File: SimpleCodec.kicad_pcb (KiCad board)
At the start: 4 copper layers, 59 x 93 mm, 119 parts, among them J1 RPI_ADC, J2 RP_GPIO, Q1 AO3401A, U1 AMS1117-5.0, U2 AMS1117-3.3, U3 NE5532, U4 NE5532, U5 NE5532, U6 NE5532, U7 NE5532, U8 CS4272, X1 PEDAL_COMBO_TOP

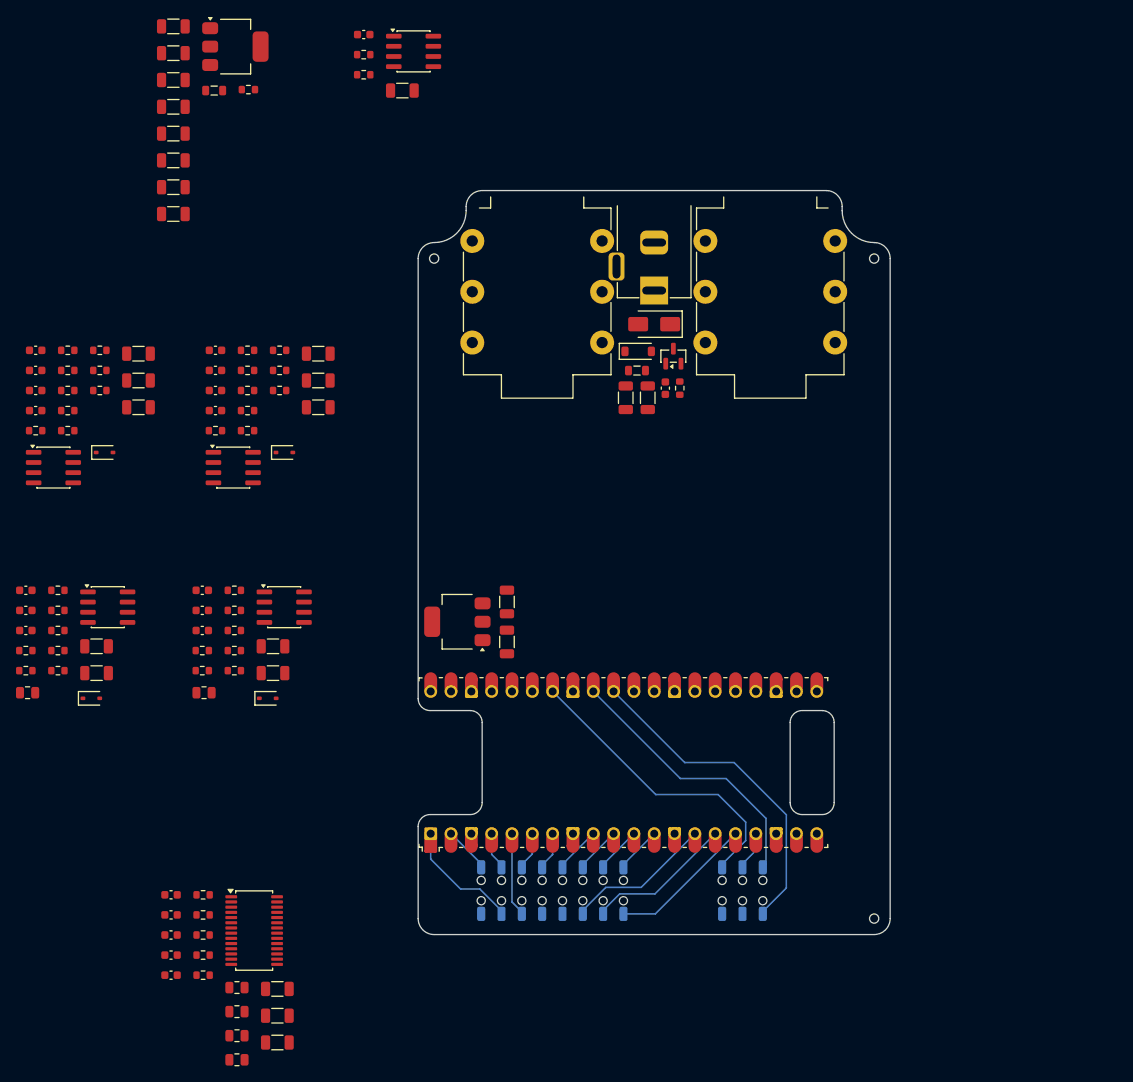
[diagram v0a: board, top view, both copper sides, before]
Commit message: Buffer and layout
Updated the input and output buffers.
Updated the board layout.
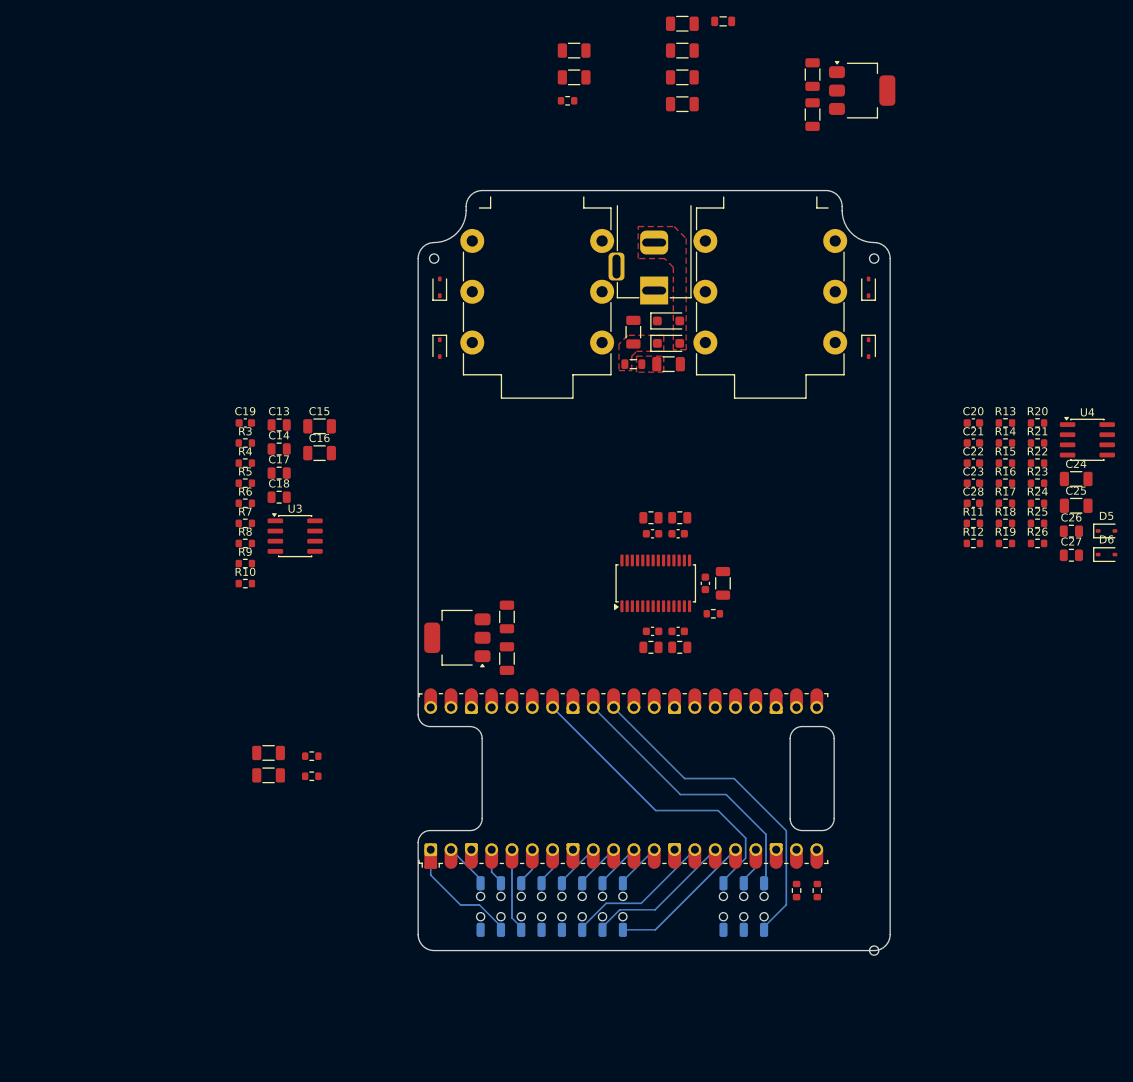
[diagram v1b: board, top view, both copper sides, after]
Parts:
- removed the C11 at (89.9, 42.1)
- removed the C2 at (151.4, 67.2)
- removed C41, C44, C45, C47, C48, C49: 100n, Capacitor_SMD:C_0603_1608Metric
- removed C42, C43, C51, C53: 1u, Capacitor_SMD:C_0805_2012Metric
- removed C46, C50: 4.7u, Capacitor_SMD:C_1206_3216Metric
- removed C52: 22u, Capacitor_SMD:C_1206_3216Metric
- removed the C8 at (89.9, 35.4)
- removed the D5 at (103.8, 75.2)
- removed the D6 at (81.3, 75.2)
- removed Q1: AO3401A, Package_TO_SOT_SMD:SOT-23
- removed R31: 22K, Resistor_SMD:R_0603_1608Metric
- removed R32, R33: 220, Resistor_SMD:R_0603_1608Metric
- removed R34, R35: 100, Resistor_SMD:R_0603_1608Metric
- removed R36, R37, R38, R39, R40, R41: 47K, Resistor_SMD:R_0603_1608Metric
- removed U6, U7: NE5532, Package_SO:SOIC-8_3.9x4.9mm_P1.27mm
- removed U8: CS4272, Package_SO:TSSOP-28_4.4x9.7mm_P0.65mm
- added C12: 22u, Capacitor_SMD:C_1206_3216Metric, F.Cu at (153.5, 31.7)
- added C6: 10u, Capacitor_SMD:C_1206_3216Metric, F.Cu at (169.8, 33.0)
- added C9: 4.7u, Capacitor_SMD:C_1206_3216Metric, F.Cu at (153.5, 25.0)
- added D5: H15VSD3B, Diode_SMD:D_SOD-323, F.Cu at (206.6, 85.0)
- added D5: H15VSD3B, Diode_SMD:D_SOD-323, F.Cu at (176.8, 62.2)
- added D6: H15VSD3B, Diode_SMD:D_SOD-323, F.Cu at (176.8, 54.6)
- added D6: H15VSD3B, Diode_SMD:D_SOD-323, F.Cu at (206.6, 88.0)
- C10: value 4.7u -> 22u
- C13: value 22u -> 2.2n; footprint Capacitor_SMD:C_1206_3216Metric -> Capacitor_SMD:C_0805_2012Metric
- C14: value 10u -> 2.2n; footprint Capacitor_SMD:C_1206_3216Metric -> Capacitor_SMD:C_0805_2012Metric
- C15: value 100n -> 10u; footprint Capacitor_SMD:C_0603_1608Metric -> Capacitor_SMD:C_1206_3216Metric
- C16: value 470p -> 10u; footprint Capacitor_SMD:C_0603_1608Metric -> Capacitor_SMD:C_1206_3216Metric
- C17: value 470p -> 2.2n; footprint Capacitor_SMD:C_0603_1608Metric -> Capacitor_SMD:C_0805_2012Metric
- C18: value 1u -> 2.2n
- C19: value 1u -> 100n; footprint Capacitor_SMD:C_0805_2012Metric -> Capacitor_SMD:C_0603_1608Metric
- C20, C21: value 2.2n -> 330p
- C22, C23: value 10u -> 330p; footprint Capacitor_SMD:C_1206_3216Metric -> Capacitor_SMD:C_0603_1608Metric
- C24, C25, C37: value 4.7u -> 10u
- C26, C27: value 100n -> 2.2n; footprint Capacitor_SMD:C_0603_1608Metric -> Capacitor_SMD:C_0805_2012Metric
- C28, C31, C36: value 4.7u -> 100n; footprint Capacitor_SMD:C_1206_3216Metric -> Capacitor_SMD:C_0603_1608Metric
- C29, C30: value 4.7u -> 1u; footprint Capacitor_SMD:C_1206_3216Metric -> Capacitor_SMD:C_0805_2012Metric
- C32, C34, C35: value 68p -> 100n
- C33: value 68p -> 10u; footprint Capacitor_SMD:C_0603_1608Metric -> Capacitor_SMD:C_1206_3216Metric
- C38: value 1n -> 1u; footprint Capacitor_SMD:C_0603_1608Metric -> Capacitor_SMD:C_0805_2012Metric
- C39: value 1n -> 22u; footprint Capacitor_SMD:C_0603_1608Metric -> Capacitor_SMD:C_1206_3216Metric
- C40: value 100n -> 1u; footprint Capacitor_SMD:C_0603_1608Metric -> Capacitor_SMD:C_0805_2012Metric
- C7: value 10u -> 4.7u
- D1: value SMAJ10CA -> SMF10CA; footprint Diode_SMD:D_SMA -> Diode_SMD:D_SOD-123F
- D2: value MMSZ5248B -> DSK24; footprint Diode_SMD:D_SOD-123 -> Diode_SMD:D_SOD-123F
- R10, R9: value 100K -> 1K
- R11: value 100K -> 15K
- R12, R13, R14: value 1K -> 15K
- R15: value 1K -> 11K
- R16: value 10K -> 11K
- R17: value 10K -> 820
- R18, R19: value 1K -> 820
- R2, R4: value 4.7K -> 100
- R20: value 100K -> 820
- R21, R22: value 100K -> 11K
- R23: value 100K -> 100
- R24: value 12K -> 100
- R25, R26, R27: value 12K -> 47K
- R28, R29, R30: value 22K -> 47K
- R5: value 4.7K -> 1M
- R6, R7: value 100 -> 1M
- R8: value 100K -> 1M
- U3, U4: value NE5532 -> MCP6002-xSN
- U5: value NE5532 -> CS4272; footprint Package_SO:SOIC-8_3.9x4.9mm_P1.27mm -> Package_SO:TSSOP-28_4.4x9.7mm_P0.65mm
- moved C26 131.3 mm to (202.2, 85.1)
- moved R22 125.3 mm to (197.9, 76.6)
- moved C24 124.8 mm to (202.8, 78.5)
- moved U4 124.2 mm to (204.2, 73.7)
- moved R26 123.1 mm to (197.9, 86.6)
- moved R23 122.4 mm to (197.9, 79.1)
- moved C20 120.7 mm to (189.9, 71.5)
- moved R14 120.7 mm to (193.9, 74.1)
- moved R16 120.3 mm to (193.9, 79.1)
- moved R18 119.9 mm to (193.9, 84.1)
- moved R12 114.7 mm to (189.9, 86.6)
- moved R27 112.6 mm to (170.4, 130.0), turned to 90 degrees
- moved C22 112.0 mm to (189.9, 76.6)
- moved C27 109.0 mm to (202.2, 88.1)
- moved R20 102.8 mm to (197.9, 71.5)
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- renumbered C12 to C11, C4 to C2, C6 to C4, C9 to C8
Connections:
- C13 pad 1: +5VA -> GND
- C13 pad 2: GND -> Net-(C13-Pad2)
- C14 pad 1: /Power/+VBIAS_RAW -> GND
- C14 pad 2: GND -> Net-(C14-Pad2)
- C15 pad 1: +VCC_FILT -> Net-(C13-Pad2)
- C15 pad 2: GND -> Net-(U3A-+)
- C16 pad 1: Net-(C16-Pad1) -> Net-(C14-Pad2)
- C16 pad 2: GND -> Net-(U3B-+)
- C17 pad 1: Net-(C17-Pad1) -> CODEC_INL
- C18 pad 1: Net-(C16-Pad1) -> CODEC_INR
- C18 pad 2: Net-(U4A-+) -> GND
- C19 pad 1: Net-(C17-Pad1) -> +5VA
- C19 pad 2: Net-(U5A-+) -> GND
- C20 pad 1: Net-(C20-Pad1) -> Net-(U4A-+)
- C20 pad 2: GND -> VCOM
- C21 pad 1: Net-(C21-Pad1) -> Net-(U4B-+)
- C21 pad 2: GND -> VCOM
- C22 pad 1: Net-(C20-Pad1) -> Net-(U4A--)
- C22 pad 2: Net-(U4B-+) -> Net-(C22-Pad2)
- C23 pad 1: Net-(C21-Pad1) -> Net-(U4B--)
- C23 pad 2: Net-(U5B-+) -> Net-(C23-Pad2)
- C24 pad 1: Net-(U4B--) -> Net-(C22-Pad2)
- C25 pad 1: Net-(U5B--) -> Net-(C23-Pad2)
- C26 pad 1: +VCC_FILT -> /Buffers_Out/AUDIO_OUTL
- C27 pad 1: +VCC_FILT -> /Buffers_Out/AUDIO_OUTR
- C28 pad 1: CODEC_OUTL- -> +5VA
- C28 pad 2: Net-(C28-Pad2) -> GND
- C29 pad 1: CODEC_OUTL+ -> GND
- C29 pad 2: Net-(C29-Pad2) -> +3V3D
- C30 pad 1: CODEC_OUTR- -> GND
- C30 pad 2: Net-(C30-Pad2) -> +3V3D
- C31 pad 1: CODEC_OUTR+ -> +3V3D
- C31 pad 2: Net-(C31-Pad2) -> GND
- C32 pad 1: Net-(U6A--) -> +3V3D
- C32 pad 2: Net-(C32-Pad2) -> GND
- C33 pad 1: Net-(U7A--) -> /Codec/INR-
- C33 pad 2: Net-(C33-Pad2) -> GND
- C34 pad 1: Net-(U6A-+) -> GND
- C34 pad 2: VBIAS_OUT -> +5VA
- C35 pad 1: Net-(U7A-+) -> VCOM
- C35 pad 2: VBIAS_OUT -> GND
- C36 pad 1: Net-(U6B--) -> /Codec/FILT+
- C36 pad 2: Net-(C36-Pad2) -> GND
- C37 pad 1: Net-(U7B--) -> /Codec/INL-
- C37 pad 2: Net-(C37-Pad2) -> GND
- C38 pad 1: /Buffers_Out/AUDIO_OUTL -> +5VA
- C39 pad 1: /Buffers_Out/AUDIO_OUTR -> VCOM
- C40 pad 1: +VCC_FILT -> GND
- C40 pad 2: GND -> /Codec/FILT+
- D1 pad 1: +VDC -> GND
- D1 pad 2: GND -> +VDC
- D2 pad 2: /Power/PROT_G -> +VDC
- R10 pad 1: Net-(U4A-+) -> Net-(U3B--)
- R10 pad 2: +VBIAS_IN -> CODEC_INR
- R11 pad 1: Net-(U5A-+) -> CODEC_OUTL-
- R11 pad 2: +VBIAS_IN -> Net-(R11-Pad2)
- R12 pad 1: Net-(U4A--) -> CODEC_OUTL+
- R12 pad 2: Net-(C20-Pad1) -> Net-(R12-Pad2)
- R13 pad 1: Net-(U5A--) -> CODEC_OUTR-
- R13 pad 2: Net-(C21-Pad1) -> Net-(R13-Pad2)
- R14 pad 1: GND -> CODEC_OUTR+
- R14 pad 2: Net-(C20-Pad1) -> Net-(R14-Pad2)
- R15 pad 1: GND -> Net-(R12-Pad2)
- R15 pad 2: Net-(C21-Pad1) -> VCOM
- R16 pad 1: Net-(U4B-+) -> Net-(R14-Pad2)
- R16 pad 2: VBIAS_IN -> VCOM
- R17 pad 1: Net-(U5B-+) -> Net-(R11-Pad2)
- R17 pad 2: VBIAS_IN -> Net-(U4A--)
- R18 pad 1: Net-(C24-Pad2) -> Net-(R12-Pad2)
- R18 pad 2: CODEC_INL -> Net-(U4A-+)
- R19 pad 1: Net-(C25-Pad2) -> Net-(R13-Pad2)
- R19 pad 2: CODEC_INR -> Net-(U4B--)
- R2 pad 1: /Power/PROT_G -> +VCC
- R2 pad 2: GND -> +VCC_FILT
- R20 pad 1: +VBIAS_OUT -> Net-(R14-Pad2)
- R20 pad 2: Net-(C28-Pad2) -> Net-(U4B-+)
- R21 pad 1: Net-(C29-Pad2) -> Net-(R11-Pad2)
- R21 pad 2: VBIAS_OUT -> Net-(C22-Pad2)
- R22 pad 1: +VBIAS_OUT -> Net-(R13-Pad2)
- R22 pad 2: Net-(C30-Pad2) -> Net-(C23-Pad2)
- R23 pad 1: Net-(C31-Pad2) -> Net-(C24-Pad2)
- R23 pad 2: VBIAS_OUT -> /Buffers_Out/AUDIO_OUTL
- R24 pad 1: Net-(C28-Pad2) -> Net-(C25-Pad2)
- R24 pad 2: Net-(U6A--) -> /Buffers_Out/AUDIO_OUTR
- R25 pad 1: Net-(C29-Pad2) -> /Buffers_Out/AUDIO_OUTL
- R25 pad 2: Net-(U6A-+) -> GND
- R26 pad 1: Net-(C30-Pad2) -> /Buffers_Out/AUDIO_OUTR
- R26 pad 2: Net-(U7A--) -> GND
- R27 pad 1: Net-(C31-Pad2) -> +3V3D
- R27 pad 2: Net-(U7A-+) -> I2C_SCL
- R28 pad 1: Net-(U6A-+) -> +3V3D
- R28 pad 2: VBIAS_OUT -> I2C_SDA
- R29 pad 1: Net-(U7A-+) -> /Codec/BMUTEC
- R29 pad 2: VBIAS_OUT -> GND
- R3 pad 1: +VCC -> /Buffers_In/AUDIO_INL
- R3 pad 2: +VCC_FILT -> Net-(C13-Pad2)
- R30 pad 1: Net-(U6A--) -> /Codec/AMUTEC
- R30 pad 2: Net-(C32-Pad2) -> GND
- R4 pad 1: +VCC_FILT -> /Buffers_In/AUDIO_INR
- R4 pad 2: /Power/+VBIAS_RAW -> Net-(C14-Pad2)
- R5 pad 1: /Power/+VBIAS_RAW -> Net-(C13-Pad2)
- R6 pad 1: /Buffers_In/AUDIO_INL -> Net-(C14-Pad2)
- R6 pad 2: Net-(C16-Pad1) -> GND
- R7 pad 1: /Buffers_In/AUDIO_INR -> Net-(U3A-+)
- R7 pad 2: Net-(C17-Pad1) -> VCOM
- R8 pad 1: GND -> Net-(U3B-+)
- R8 pad 2: Net-(C16-Pad1) -> VCOM
- R9 pad 1: GND -> Net-(U3A--)
- R9 pad 2: Net-(C17-Pad1) -> CODEC_INL
- U3 pad 1: +VBIAS_IN -> Net-(U3A--)
- U3 pad 2: +VBIAS_IN -> Net-(U3A--)
- U3 pad 3: /Power/+VBIAS_RAW -> Net-(U3A-+)
- U3 pad 5: /Power/+VBIAS_RAW -> Net-(U3B-+)
- U3 pad 6: +VBIAS_OUT -> Net-(U3B--)
- U3 pad 7: +VBIAS_OUT -> Net-(U3B--)
- U3 pad 8: +VCC_FILT -> +5VA
- U4 pad 1: Net-(U4A--) -> Net-(C22-Pad2)
- U4 pad 7: Net-(U4B--) -> Net-(C23-Pad2)
- U4 pad 8: +VCC_FILT -> +5VA
- U5 pad 1: Net-(U5A--) -> unconnected-(U5-XT0-Pad1)
- U5 pad 2: Net-(U5A--) -> unconnected-(U5-XTI-Pad2)
- U5 pad 3: Net-(U5A-+) -> I2S_MCLK
- U5 pad 4: GND -> I2S_LRCK
- U5 pad 5: Net-(U5B-+) -> I2S_SCLK
- U5 pad 6: Net-(U5B--) -> I2S_SDOUT
- U5 pad 7: Net-(U5B--) -> I2S_SDIN
- U5 pad 8: +VCC_FILT -> GND
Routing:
- added copper zone on F.Cu, net +VCC
- added copper zone on F.Cu, net +VDC
- added copper zone on F.Cu, net +VDC_PROT
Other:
- board size 59 x 93 mm -> 59 x 95 mm
